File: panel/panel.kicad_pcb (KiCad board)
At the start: 2 copper layers, 20.3 x 128.5 mm, 0 parts

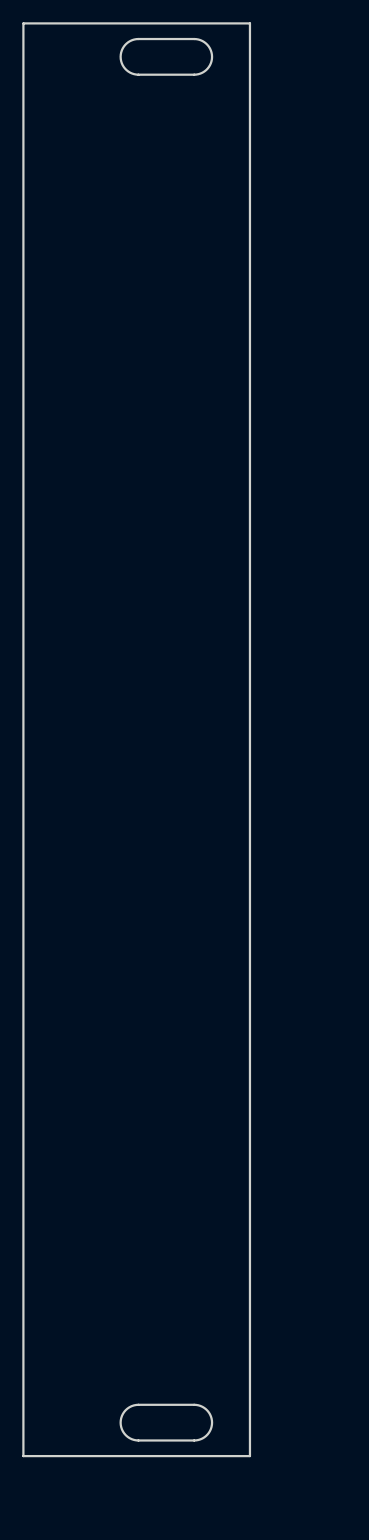
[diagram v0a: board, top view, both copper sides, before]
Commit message: holes for panel, set origin for board
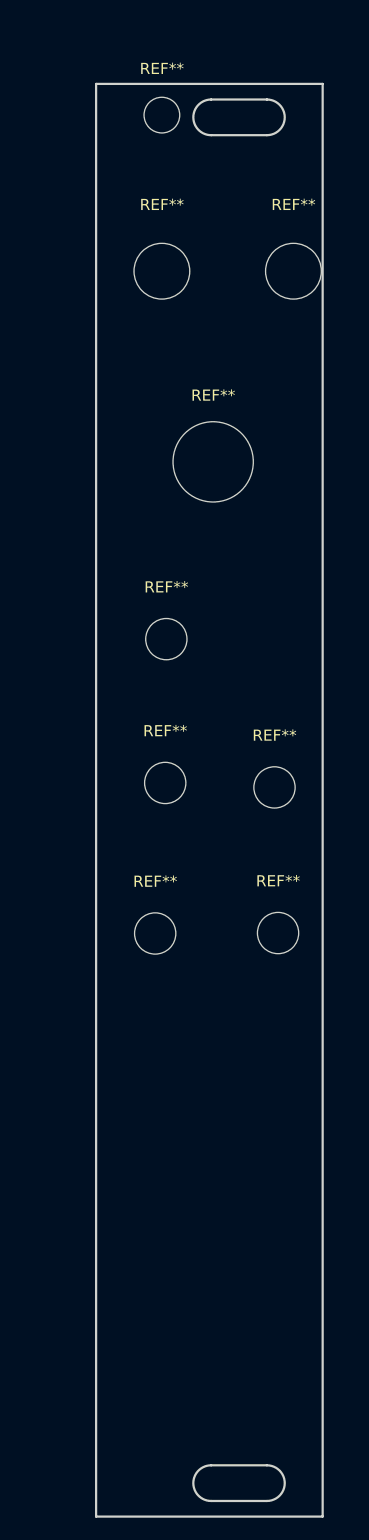
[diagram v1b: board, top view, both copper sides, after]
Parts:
- added REF**: MountingHole_3.7mm, MountingHole:MountingHole_3.7mm, F.Cu at (166.0, 94.6)
- added REF**: MountingHole_7.2mm, drichert:MountingHole_7.2mm, F.Cu at (160.5, 65.4)
- added REF**: MountingHole_5mm, MountingHole:MountingHole_5mm, F.Cu at (155.9, 48.3)
- added REF**: MountingHole_3.7mm, MountingHole:MountingHole_3.7mm, F.Cu at (155.3, 107.7)
- added REF**: MountingHole_3.7mm, MountingHole:MountingHole_3.7mm, F.Cu at (156.2, 94.2)
- added REF**: MountingHole_3.7mm, MountingHole:MountingHole_3.7mm, F.Cu at (156.3, 81.3)
- added REF**: MountingHole_3.7mm, MountingHole:MountingHole_3.7mm, F.Cu at (166.3, 107.7)
- added REF**: MountingHole_5mm, MountingHole:MountingHole_5mm, F.Cu at (167.7, 48.3)
- added REF**: MountingHole_3.2mm_M3, MountingHole:MountingHole_3.2mm_M3, F.Cu at (155.9, 34.3)

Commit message: holes
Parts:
- moved REF** 31.4 mm to (165.2, 139.0)
- moved REF** 31.3 mm to (155.2, 139.0)
- moved REF** 30.4 mm to (155.2, 124.6)
- moved REF** 30.0 mm to (165.2, 124.6)
- moved REF** 28.9 mm to (155.2, 110.2)
- moved REF** 21.6 mm to (155.8, 55.9)
- moved REF** 20.1 mm to (164.2, 68.1)
- moved REF** 19.8 mm to (156.3, 68.1)
- moved REF** 18.3 mm to (160.2, 83.7)
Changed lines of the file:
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@@
 	(footprint "MountingHole:MountingHole_3.7mm"
 		(layer "F.Cu")
-		(at 166 94.6)
+		(at 165.16 124.63)
 		(descr "Mounting Hole 3.7mm, no annular, generated by kicad-footprint-generator mountinghole.py")
 		(tags "mountinghole")
@@
 			(at 0 -4.65 0)
 			(layer "F.SilkS")
+			(hide yes)
 			(effects
 				(font
@@
 			(at 0 4.65 0)
 			(layer "F.Fab")
+			(hide yes)
 			(effects
 				(font
@@
 	(footprint "drichert:MountingHole_7.2mm"
 		(layer "F.Cu")
-		(at 160.5 65.4)
+		(at 160.16 83.725)
 		(descr "Mounting Hole 5mm, no annular, generated by kicad-footprint-generator mountinghole.py")
 		(tags "mountinghole")
@@
 			(at 0 -5.95 0)
 			(layer "F.SilkS")
+			(hide yes)
 			(effects
 				(font
@@
 			(at 0 5.95 0)
 			(layer "F.Fab")
+			(hide yes)
 			(effects
 				(font
@@
 	(footprint "MountingHole:MountingHole_5mm"
 		(layer "F.Cu")
-		(at 155.9 48.3)
+		(at 156.26 68.0574)
 		(descr "Mounting Hole 5mm, no annular, generated by kicad-footprint-generator mountinghole.py")
 		(tags "mountinghole")
@@
 			(at 0 -5.95 0)
 			(layer "F.SilkS")
+			(hide yes)
 			(effects
 				(font
@@
 			(at 0 5.95 0)
 			(layer "F.Fab")
+			(hide yes)
 			(effects
 				(font
@@
 	(footprint "MountingHole:MountingHole_3.7mm"
 		(layer "F.Cu")
-		(at 155.3 107.7)
+		(at 155.16 139.03)
 		(descr "Mounting Hole 3.7mm, no annular, generated by kicad-footprint-generator mountinghole.py")
 		(tags "mountinghole")
@@
 			(at 0 -4.65 0)
 			(layer "F.SilkS")
+			(hide yes)
 			(effects
 				(font
@@
 			(at 0 4.65 0)
 			(layer "F.Fab")
+			(hide yes)
 			(effects
 				(font
@@
 	(footprint "MountingHole:MountingHole_3.7mm"
 		(layer "F.Cu")
-		(at 156.2 94.2)
+		(at 155.16 124.63)
 		(descr "Mounting Hole 3.7mm, no annular, generated by kicad-footprint-generator mountinghole.py")
 		(tags "mountinghole")
@@
 			(at 0 -4.65 0)
 			(layer "F.SilkS")
+			(hide yes)
 			(effects
 				(font
@@
 			(at 0 4.65 0)
 			(layer "F.Fab")
+			(hide yes)
 			(effects
 				(font
@@
 	(footprint "MountingHole:MountingHole_3.7mm"
 		(layer "F.Cu")
-		(at 156.3 81.3)
+		(at 155.16 110.2)
 		(descr "Mounting Hole 3.7mm, no annular, generated by kicad-footprint-generator mountinghole.py")
 		(tags "mountinghole")
@@
 			(at 0 -4.65 0)
 			(layer "F.SilkS")
+			(hide yes)
 			(effects
 				(font
@@
 			(at 0 4.65 0)
 			(layer "F.Fab")
+			(hide yes)
 			(effects
 				(font
@@
 	(footprint "MountingHole:MountingHole_3.7mm"
 		(layer "F.Cu")
-		(at 166.320416 107.661083)
+		(at 165.16 139.03)
 		(descr "Mounting Hole 3.7mm, no annular, generated by kicad-footprint-generator mountinghole.py")
 		(tags "mountinghole")
@@
 			(at 0 -4.65 0)
 			(layer "F.SilkS")
+			(hide yes)
 			(effects
 				(font
@@
 			(at 0 4.65 0)
 			(layer "F.Fab")
+			(hide yes)
 			(effects
 				(font
@@
 	(footprint "MountingHole:MountingHole_5mm"
 		(layer "F.Cu")
-		(at 167.7 48.3)
+		(at 164.1595 68.0574)
 		(descr "Mounting Hole 5mm, no annular, generated by kicad-footprint-generator mountinghole.py")
 		(tags "mountinghole")
@@
 			(at 0 -5.95 0)
 			(layer "F.SilkS")
+			(hide yes)
 			(effects
 				(font
@@
 			(at 0 5.95 0)
 			(layer "F.Fab")
+			(hide yes)
 			(effects
 				(font
@@
 	(footprint "MountingHole:MountingHole_3.2mm_M3"
 		(layer "F.Cu")
-		(at 155.9 34.3)
+		(at 155.76 55.85)
 		(descr "Mounting Hole 3.2mm, M3, no annular, generated by kicad-footprint-generator mountinghole.py")
 		(tags "mountinghole M3")
@@
 			(at 0 -4.15 0)
 			(layer "F.SilkS")
+			(hide yes)
 			(effects
 				(font
@@
 			(at 0 4.15 0)
 			(layer "F.Fab")
+			(hide yes)
 			(effects
 				(font
@@
 	)
 	(group ""
+		(members "505e7fef-8a4f-4ea2-83a8-1357386b8bf8" "52264f0f-3626-44fc-a4fb-6006f6ee6ea1"
+			"6033d4d5-3435-41ff-9703-8c4bf459a60a" "746f9d47-13cc-4041-b93c-8d060502b68a"
+			"75860c5e-9c35-4e06-aed1-77c2bf73cde1" "8ca7b818-eb89-42e0-9154-101a45b7c451"
+			"8d6e7428-ceb9-4509-a9de-d62f92518eb7" "9c86ffef-8b24-4230-bea3-a7b9a644101d"
+			"eb774107-4bbe-44ea-a491-5e1aa6be9062"
+		)
+	)
+	(group ""

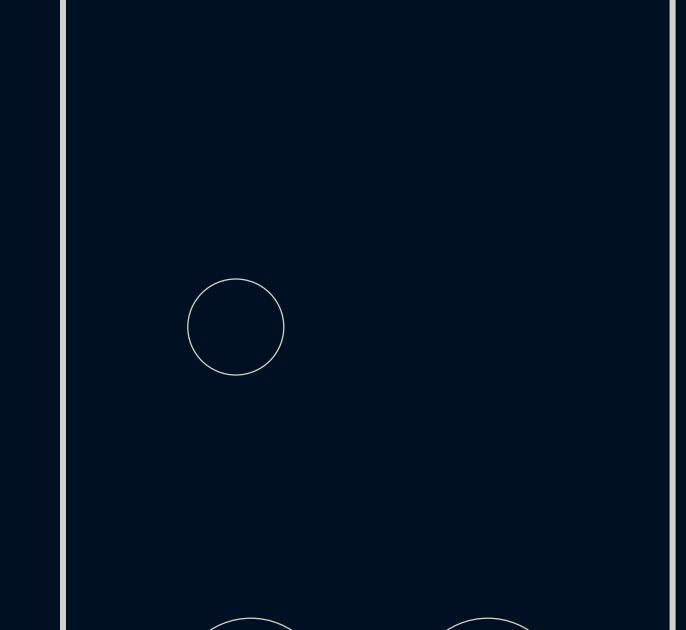
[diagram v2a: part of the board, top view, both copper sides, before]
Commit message: tht film cap, move standoff hole
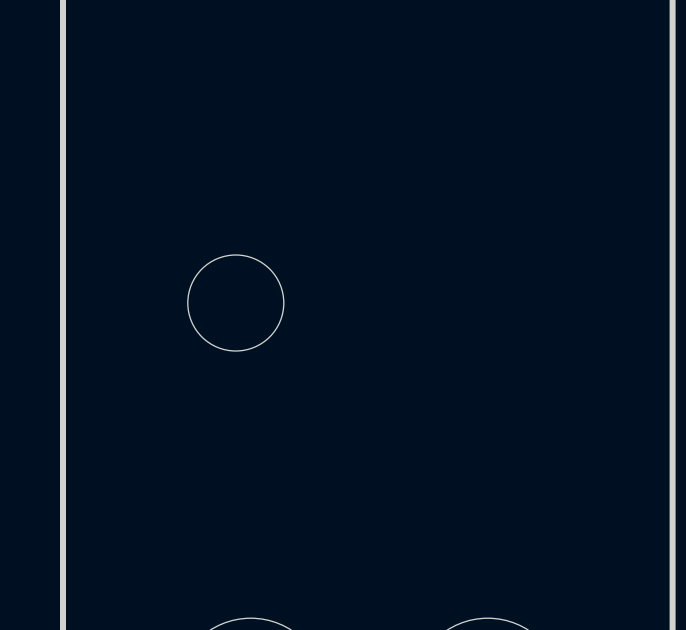
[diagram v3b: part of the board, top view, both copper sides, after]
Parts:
- moved REF** 0.80 mm to (155.8, 55.0)
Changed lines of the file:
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@@
 	(footprint "MountingHole:MountingHole_3.2mm_M3"
 		(layer "F.Cu")
-		(at 155.76 55.85)
+		(at 155.76 55.05)
 		(descr "Mounting Hole 3.2mm, M3, no annular, generated by kicad-footprint-generator mountinghole.py")
 		(tags "mountinghole M3")

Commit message: wip
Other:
- board text added: "12mm knob"
- board text added: "AC"
- board text added: "BOOST ON"
- board text added: "BOOSTMULT"
- board text added: "DC"
- board text added: "GAIN"
- board text added: "IN"
- board text added: "NO BOOST"
- board text added: "OUT1"
- board text added: "OUT2"
- board text added: "OUT3"
- board text added: "OUT4"
